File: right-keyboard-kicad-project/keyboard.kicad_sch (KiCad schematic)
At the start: 106 parts, among them U1 TRRS, U2 Arduino_Pro_Micro

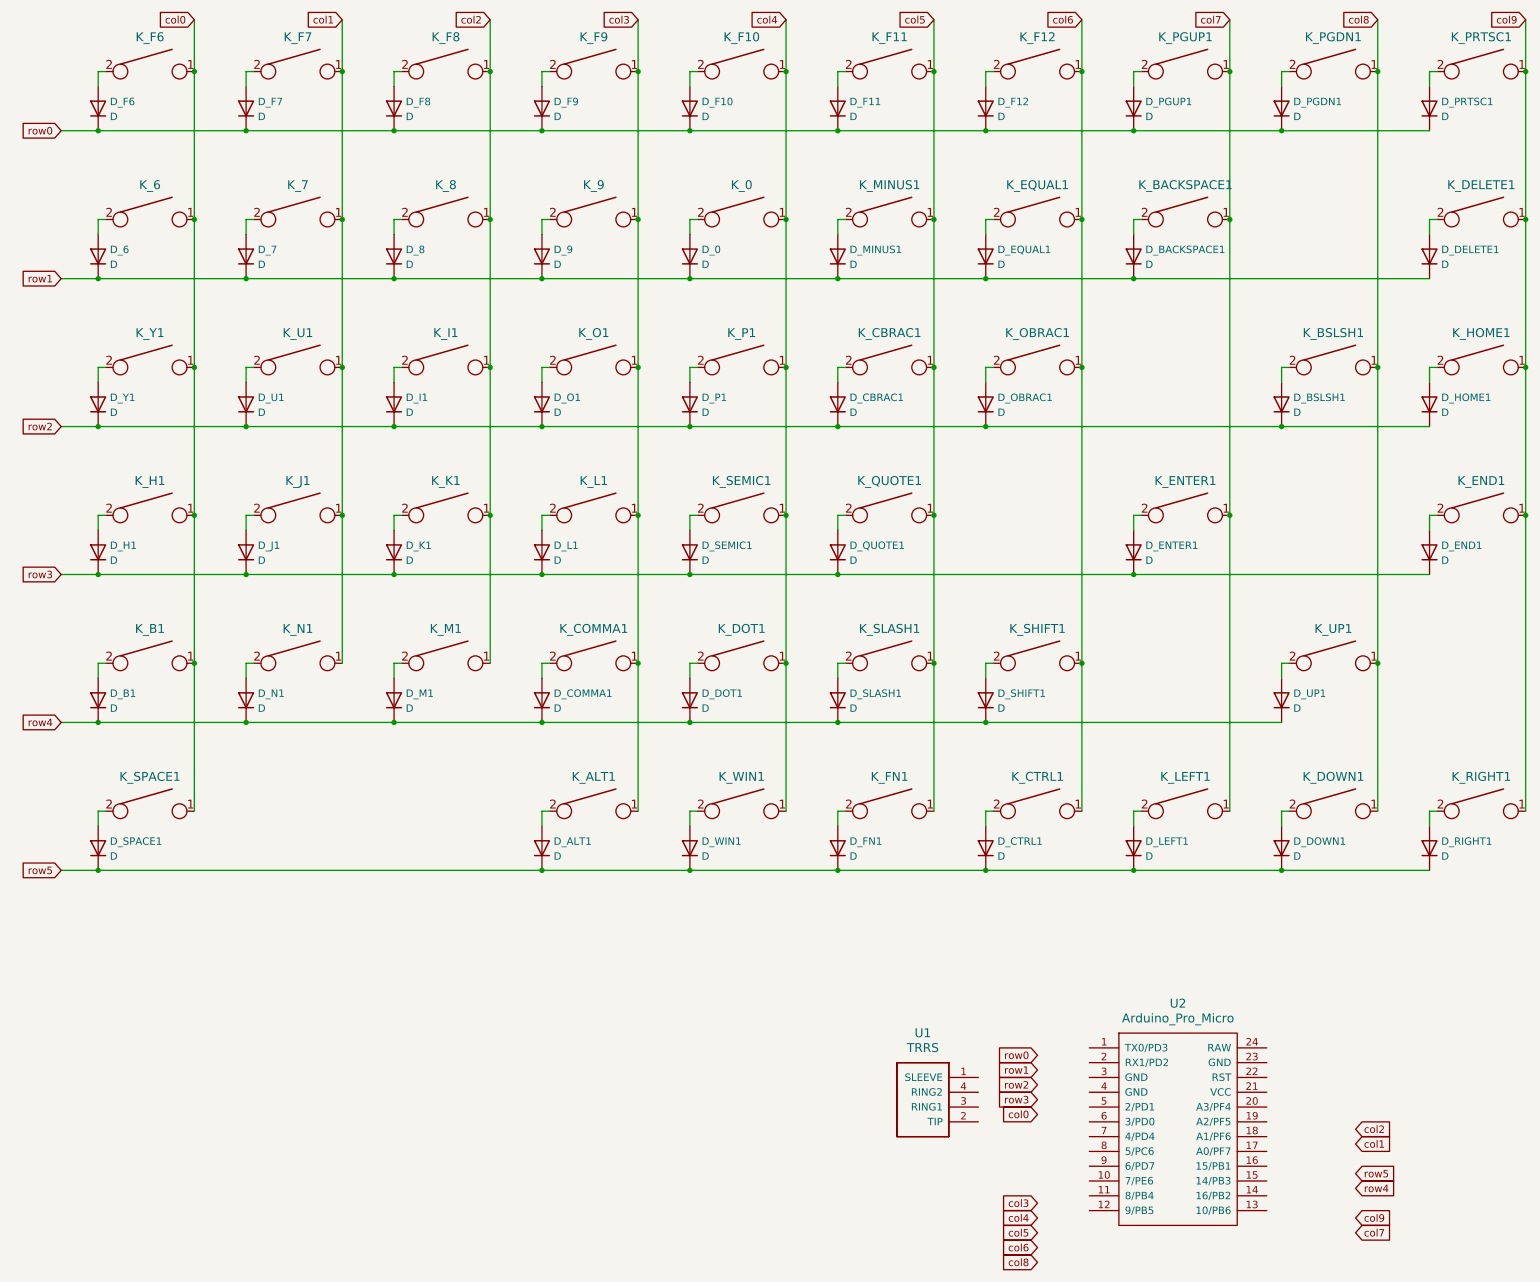
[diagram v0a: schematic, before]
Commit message: Redid right keyboard firmware wiring and started right keyboard Kicad project
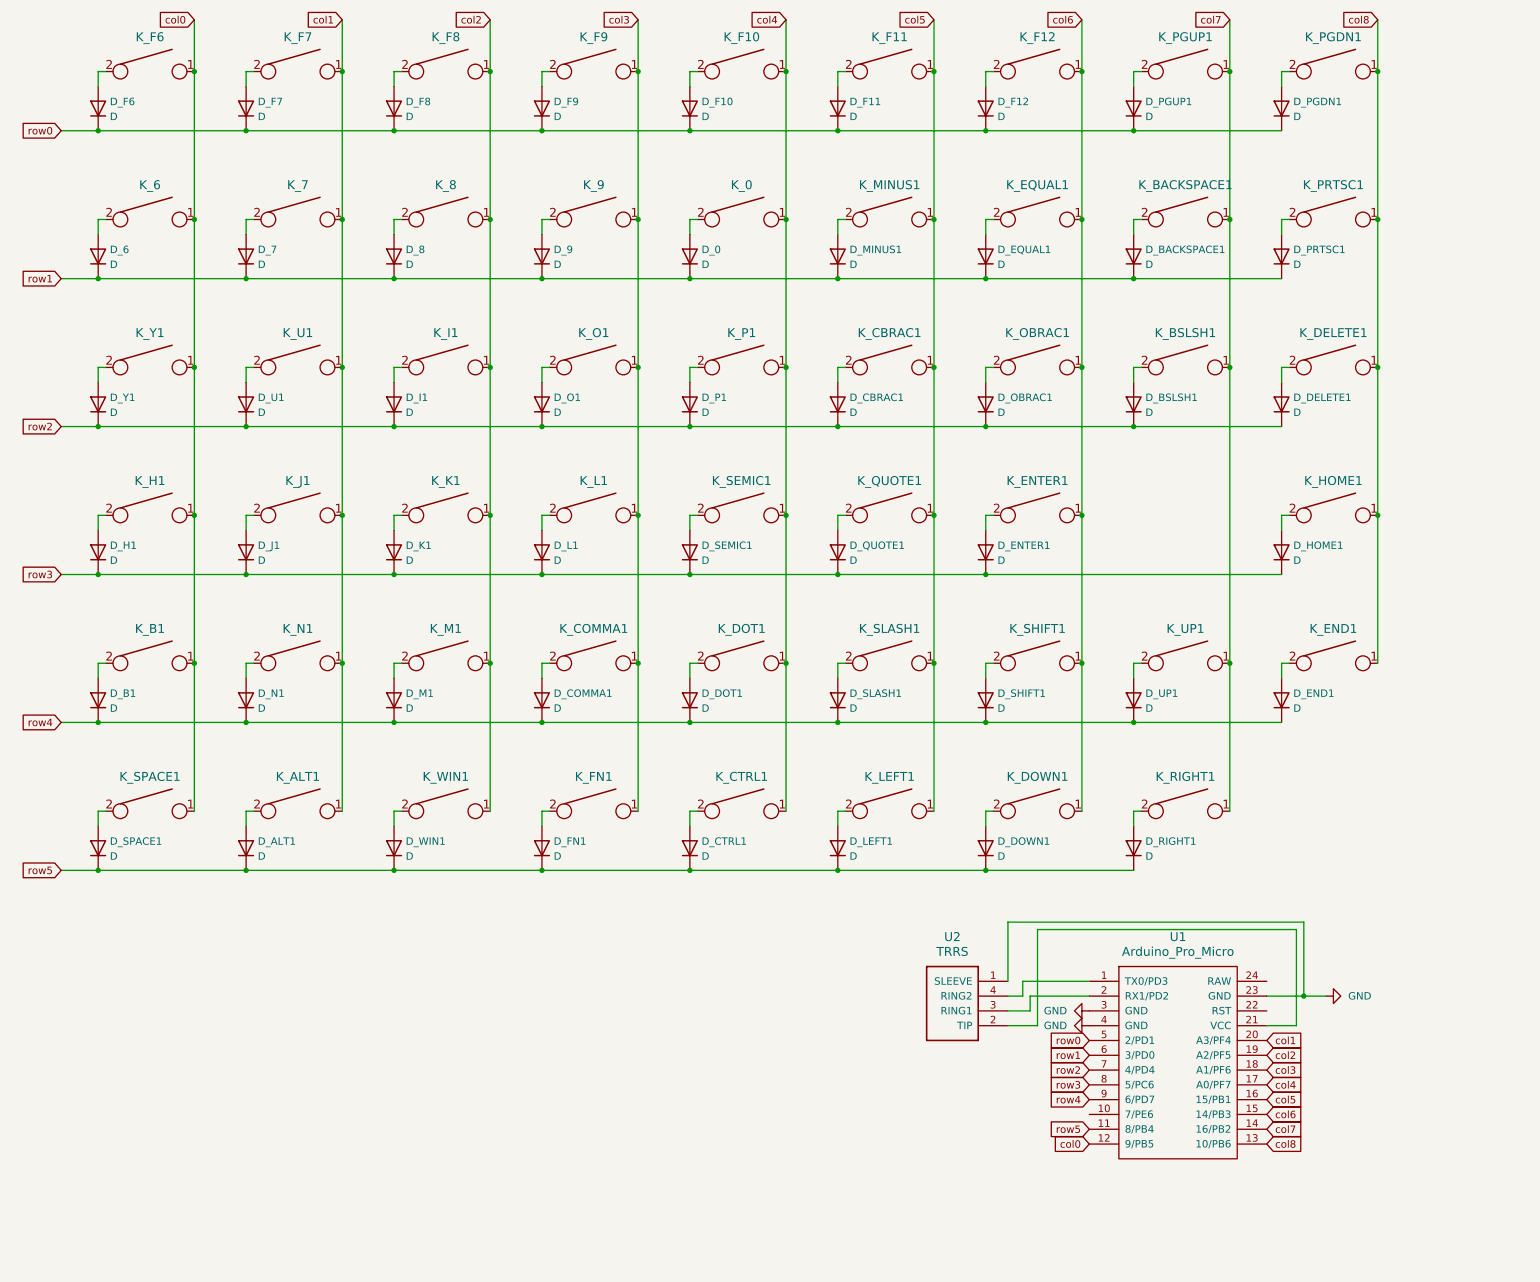
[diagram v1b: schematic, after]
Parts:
- removed U1: TRRS, ScottoKeebs_Components:TRRS_PJ-320A, symbol ScottoKeebs:Placeholder_TRRS
- removed U2: Arduino_Pro_Micro, ScottoKeebs_MCU:Arduino_Pro_Micro, symbol ScottoKeebs:MCU_Arduino_Pro_Micro
- added U1: Arduino_Pro_Micro, ScottoKeebs_MCU:Arduino_Pro_Micro, symbol ScottoKeebs:MCU_Arduino_Pro_Micro
- added U2: TRRS, ScottoKeebs_Components:TRRS_PJ-320A, symbol ScottoKeebs:Placeholder_TRRS
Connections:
- net col0: now also U1.12 (9/PB5)
- net col1: now also K_ALT1.1, U1.20 (A3/PF4)
- net col2: now also K_WIN1.1, U1.19 (A2/PF5)
- net col3: now also K_FN1.1, U1.18 (A1/PF6); no longer K_ALT1.1
- net col4: now also K_CTRL1.1, U1.17 (A0/PF7); no longer K_WIN1.1
- net col5: now also K_LEFT1.1, U1.16 (15/PB1); no longer K_FN1.1
- net col6: now also K_DOWN1.1, K_ENTER1.1, U1.15 (14/PB3); no longer K_CTRL1.1
- net col7: now also K_BSLSH1.1, K_RIGHT1.1, K_UP1.1, U1.14 (16/PB2); no longer K_ENTER1.1, K_LEFT1.1
- net col8: now also K_DELETE1.1, K_END1.1, K_HOME1.1, K_PRTSC1.1, U1.13 (10/PB6); no longer K_BSLSH1.1, K_DOWN1.1, K_UP1.1
- net row0: now also U1.5 (2/PD1); no longer D_PRTSC1.1 (K)
- net row1: now also D_PRTSC1.1 (K), U1.6 (3/PD0); no longer D_DELETE1.1 (K)
- net row2: now also D_DELETE1.1 (K), U1.7 (4/PD4); no longer D_HOME1.1 (K)
- net row3: now also D_HOME1.1 (K), U1.8 (5/PC6); no longer D_END1.1 (K)
- net row4: now also D_END1.1 (K), U1.9 (6/PD7)
- net row5: now also U1.11 (8/PB4)
- removed net col9: K_DELETE1.1, K_END1.1, K_HOME1.1, K_PRTSC1.1, K_RIGHT1.1
- new net: U1.1 (TX0/PD3), U2.4 (RING2)
- new net: U1.2 (RX1/PD2), U2.3 (RING1)
- new net: U1.21 (VCC), U2.2 (TIP)
- new net GND: U1.23 (GND), U1.3 (GND), U1.4 (GND), U2.1 (SLEEVE)
